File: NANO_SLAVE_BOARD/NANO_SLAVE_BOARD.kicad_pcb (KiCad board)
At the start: 2 copper layers, 69.4 x 49.1 mm, 24 parts, among them J1 RJ45_SHIELDED, P1 CONN_02X05, P2 CONN_02X05, P3 CONN_01X05, P4 CONN_01X05, P5 CONN_02X05, Q1 BSS138, Q2 BSS138, Q3 BSS138, Q4 BSS138, Q5 BSS138, U1 arduino_nano

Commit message: routing fixes
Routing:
- net D3: track 88.6 -> 86.7 mm
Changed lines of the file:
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@@
     (thickness 1.6)
     (drawings 14)
-    (tracks 454)
+    (tracks 451)
     (zones 0)
     (modules 24)
@@
   (segment (start 146.177 113.792) (end 144.526 114.173) (width 0.3) (layer F.Cu) (net 23))
   (segment (start 146.177 113.792) (end 147.32 112.395) (width 0.3) (layer F.Cu) (net 23))
-  (segment (start 128.27 101.219) (end 128.27 93.091) (width 0.3) (layer B.Cu) (net 24))
   (segment (start 149.86 127.127) (end 148.336 125.603) (width 0.3) (layer F.Cu) (net 24))
   (segment (start 137.368972 125.603) (end 125.222 126.746) (width 0.3) (layer F.Cu) (net 24))
@@
   (segment (start 125.349 126.746) (end 122.047 121.412) (width 0.3) (layer B.Cu) (net 24))
   (segment (start 122.047 121.412) (end 124.968 103.378) (width 0.3) (layer B.Cu) (net 24))
-  (segment (start 124.968 103.378) (end 128.27 101.219) (width 0.3) (layer B.Cu) (net 24))
+  (segment (start 124.968 103.378) (end 133.858 84.582) (width 0.3) (layer B.Cu) (net 24))
   (segment (start 142.685 83.82) (end 147.13 88.265) (width 0.3) (layer B.Cu) (net 24))
   (segment (start 134.62 83.82) (end 142.685 83.82) (width 0.3) (layer B.Cu) (net 24))
   (segment (start 133.858 84.582) (end 134.62 83.82) (width 0.3) (layer B.Cu) (net 24))
-  (segment (start 131.064 91.313) (end 133.858 84.582) (width 0.3) (layer B.Cu) (net 24))
-  (segment (start 128.27 93.091) (end 131.064 91.313) (width 0.3) (layer B.Cu) (net 24))
   (segment (start 149.86 127.635) (end 149.86 127.127) (width 0.3) (layer F.Cu) (net 24))
   (segment (start 172.72 127.635) (end 172.72 124.333) (width 0.3) (layer F.Cu) (net 26))

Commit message: suggested changes
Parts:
- added REF**: MountingHole_2.7mm_M2.5, Mounting_Holes:MountingHole_2.7mm_M2.5, F.Cu at (118.4, 125.1)
- added REF**: MountingHole_2.7mm_M2.5, Mounting_Holes:MountingHole_2.7mm_M2.5, F.Cu at (178.6, 125.1)
- added REF**: MountingHole_2.7mm_M2.5, Mounting_Holes:MountingHole_2.7mm_M2.5, F.Cu at (167.8, 83.8)
- added REF**: MountingHole_2.7mm_M2.5, Mounting_Holes:MountingHole_2.7mm_M2.5, F.Cu at (129.2, 83.8)
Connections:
- P5 pad 3: S_Q8 -> S_Q6
- P5 pad 5: S_Q6 -> S_Q8
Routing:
- net SCL: track 110.4 -> 93.8 mm, vias 4 -> 5
- net +5V: track 156.9 -> 141.3 mm, vias 9 -> 5
- net S_CS: track 50.4 -> 35.2 mm, vias 2 -> 0
- net +3V3: track 81.9 -> 75.4 mm, vias 5 -> 6
- net SDA: track 116.5 -> 110.1 mm, vias 3 -> 4
- net D6: track 43.1 -> 37.2 mm, vias 0 -> 2
- net S_SCK: track 49.0 -> 43.5 mm, vias 0 -> 2
- net D5: track 45.5 -> 40.9 mm, vias 0 -> 2
- net A0: track 44.2 -> 39.9 mm, vias 0 -> 1
- net A2: track 35.3 -> 31.1 mm, vias 0 -> 1
- net A1: track 39.7 -> 35.5 mm, vias 0 -> 1
- net S_MOSI: track 41.9 -> 37.9 mm, vias 1 -> 0
- net S_MISO: track 40.5 -> 44.3 mm, vias 2 -> 0
- net S_Q6: track 37.0 -> 40.0 mm
- net D3: track 86.7 -> 89.5 mm, vias 1 -> 2
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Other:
- outline, holes or cut-outs redrawn
- net class .25: trace_width 0.3 -> 0.25

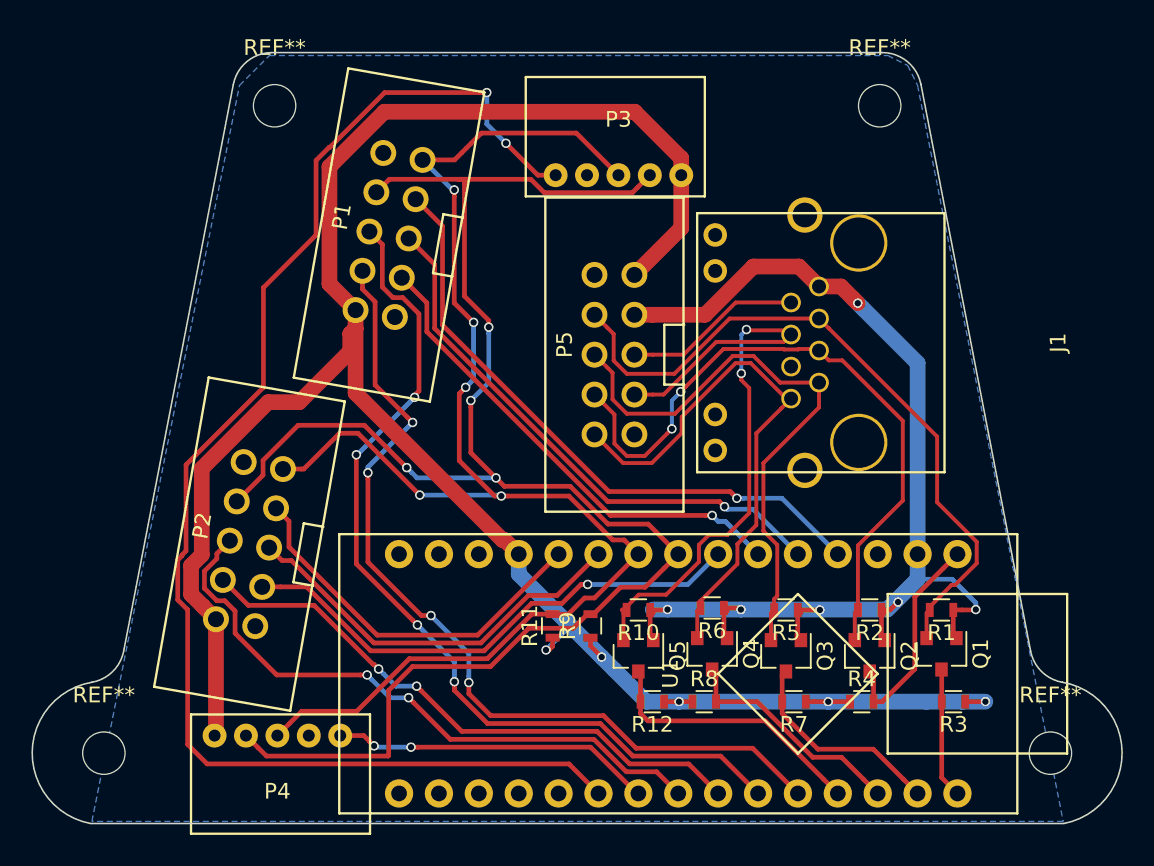
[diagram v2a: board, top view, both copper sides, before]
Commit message: added silkscreen
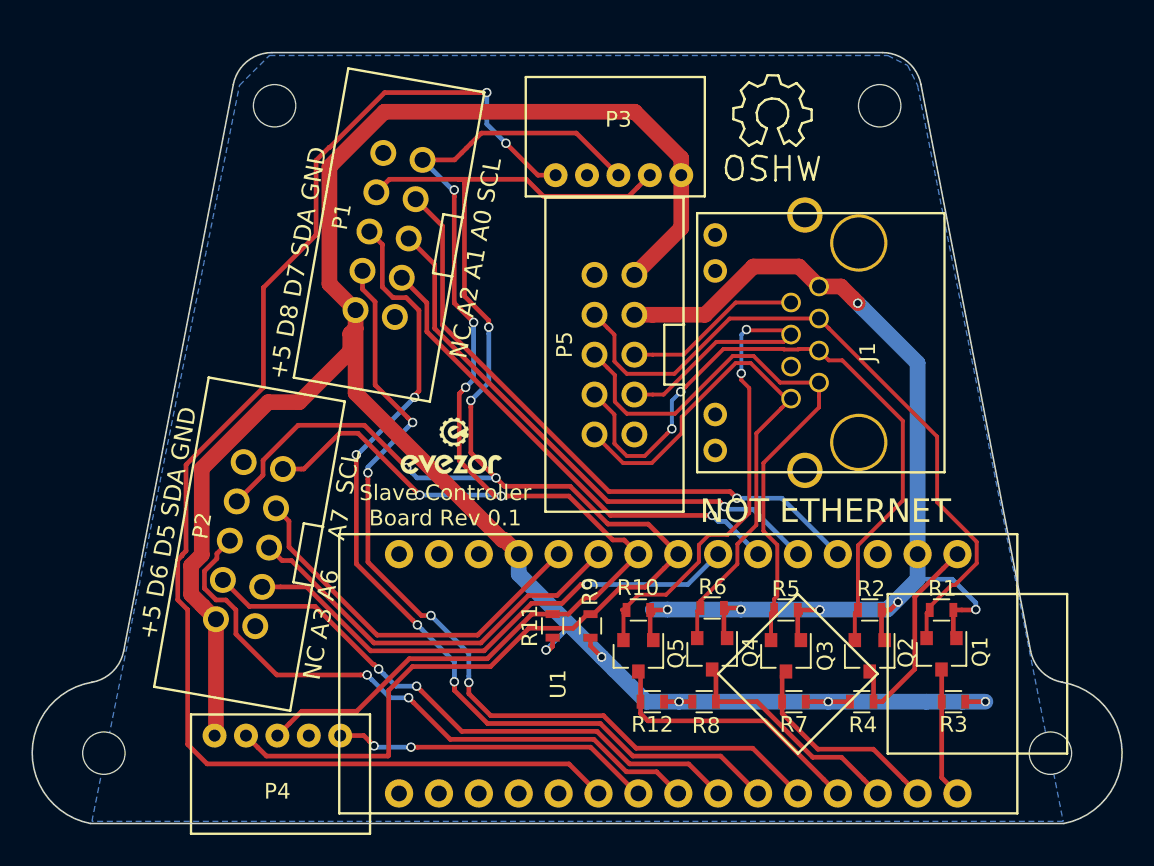
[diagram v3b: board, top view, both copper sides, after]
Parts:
- added G***: LOGO, ASSETS:evezor_12, F.Cu at (140.5, 106.7)
- added G***: LOGO, ASSETS:GEAR_18, F.Cu at (140.7, 104.6)
- added REF**: Symbol_OSHW-Logo_SilkScreen, ASSETS:Symbol_OSHW-Logo_SilkScreen, F.Cu at (160.9, 84.4)
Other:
- board text added: "+5 D6 D5 SDA GND"
- board text added: "+5 D8 D7 SDA GND"
- board text added: "NC A2 A1 A0 SCL"
- board text added: "NC A3 A6 A7 SCL"
- board text added: "NOT ETHERNET"
- board text added: "Slave Controller Board Rev 0.1"

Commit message: orientation fix
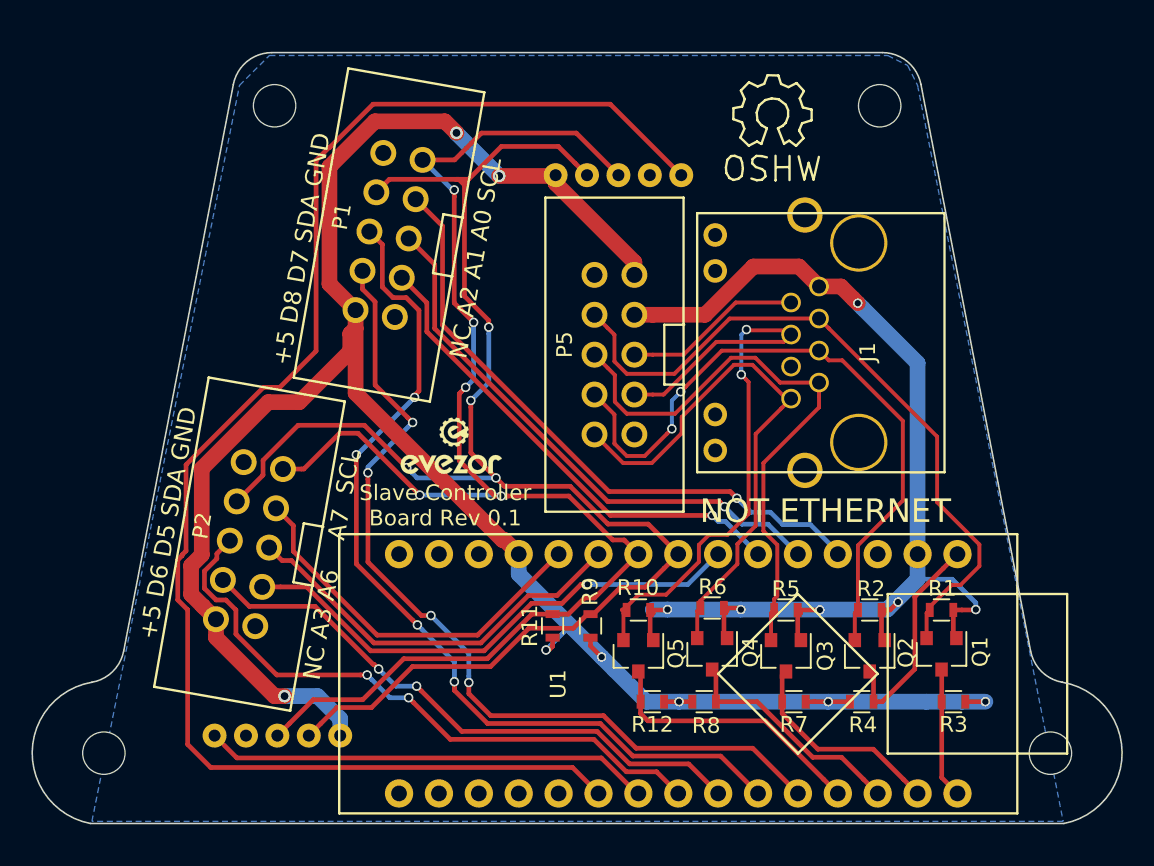
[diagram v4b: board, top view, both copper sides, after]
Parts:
- P3, P4: moved to B.Cu
- turned P3 to 0 degrees
- turned P4 to 180 degrees
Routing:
- net SDA: track 110.3 -> 99.9 mm
- net D4: track 20.8 -> 27.9 mm, vias 2 -> 0
- net D3: track 89.5 -> 96.3 mm, vias 2 -> 0
- net +5V: track 141.3 -> 138.0 mm, vias 5 -> 8

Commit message: Reroutings
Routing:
- net S_MOSI: track 37.8 -> 46.9 mm
- net S_CS: track 35.1 -> 43.0 mm
- net S_Q6: track 40.0 -> 47.5 mm
- net S_SCK: track 43.3 -> 46.4 mm
- net D3: track 96.3 -> 95.7 mm
- net A2: vias 1 -> 0
- net A1: vias 1 -> 0
